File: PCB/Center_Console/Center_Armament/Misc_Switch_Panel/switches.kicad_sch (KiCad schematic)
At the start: 8 parts, among them SW1 FUEL_EXT_BTN, SW2 MASTER_TEST, SW3 RADAR_PROFILE, SW4 RADAR_RANGE, SW5 CONT_NORM, SW6 BDHI_MODE, SW7 SW_Rotary_1x5_MP

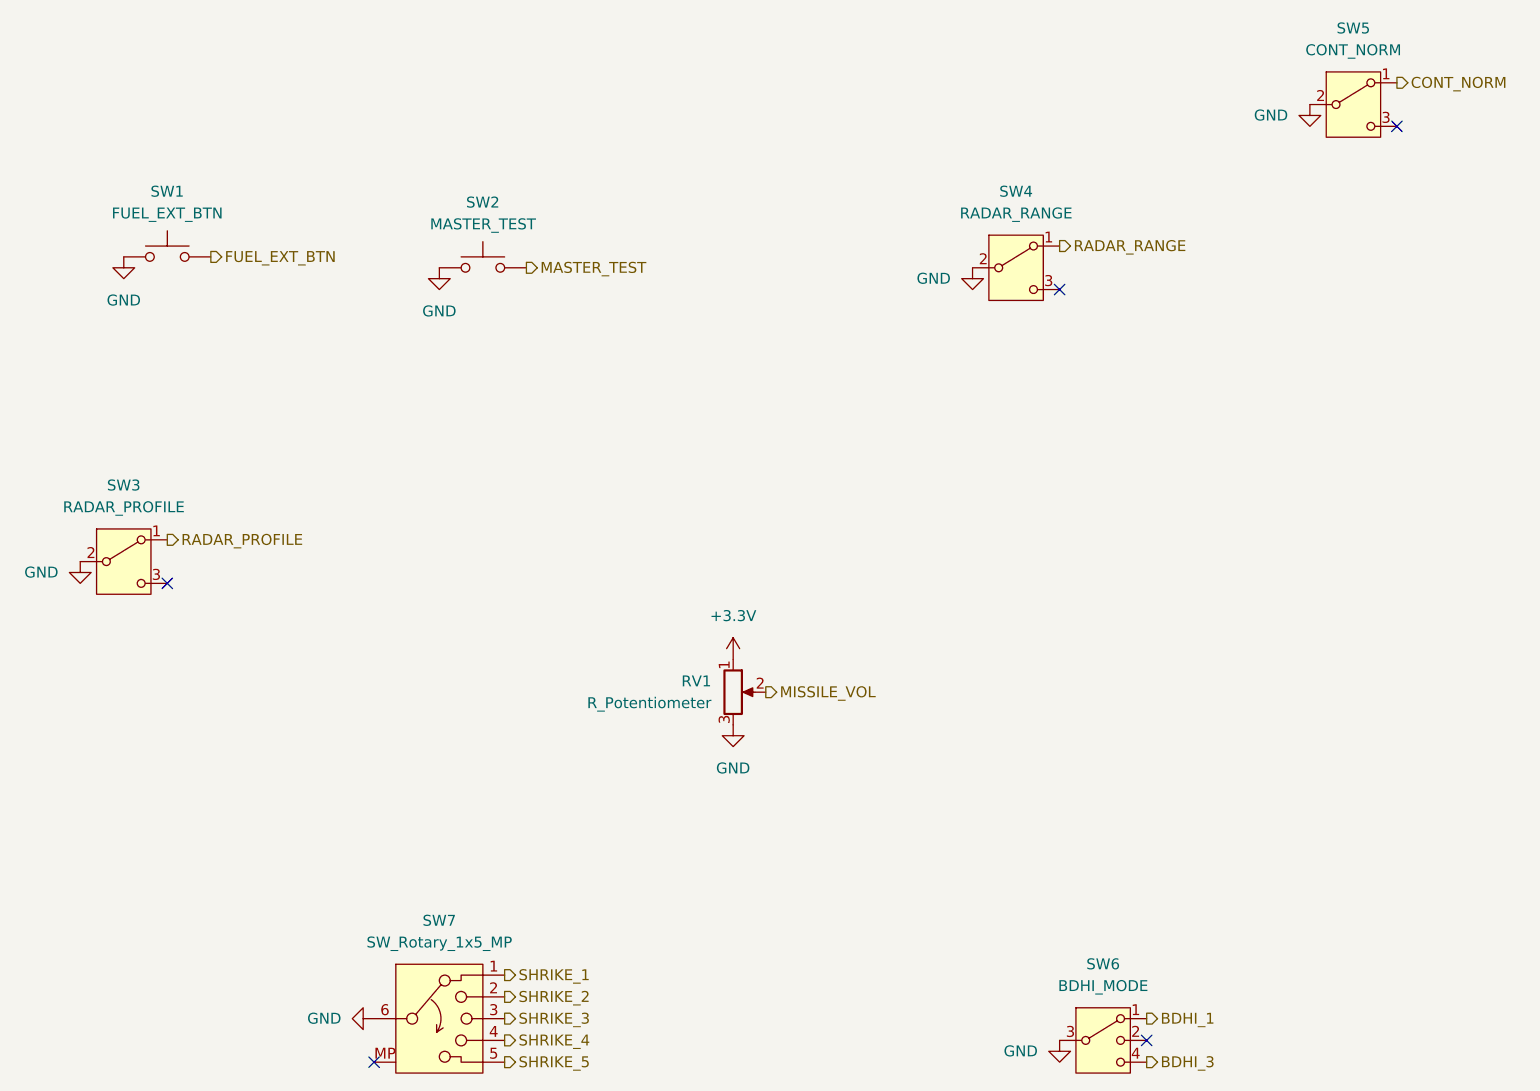
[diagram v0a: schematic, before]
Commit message: Fix LED_5050_Red symbol polarity: K=pin1, A=pin2
Symbol body was mirrored vs standard Device:LED convention — pin 1 was
labelled A and pin 2 K. Flipped triangle/bar to point left and swapped
pin names so K=1 (left) and A=2 (right), matching the generic KiCad LED
symbol.

Physical LED verified: notched/chamfered corner is the ANODE. Footprint
pad positions unchanged — pad2 (left, where the silkscreen marker sits)
is now correctly the anode. Updated kicad.md to document this.

Also includes Misc_Switch_Panel schematic edits from current KiCad session.
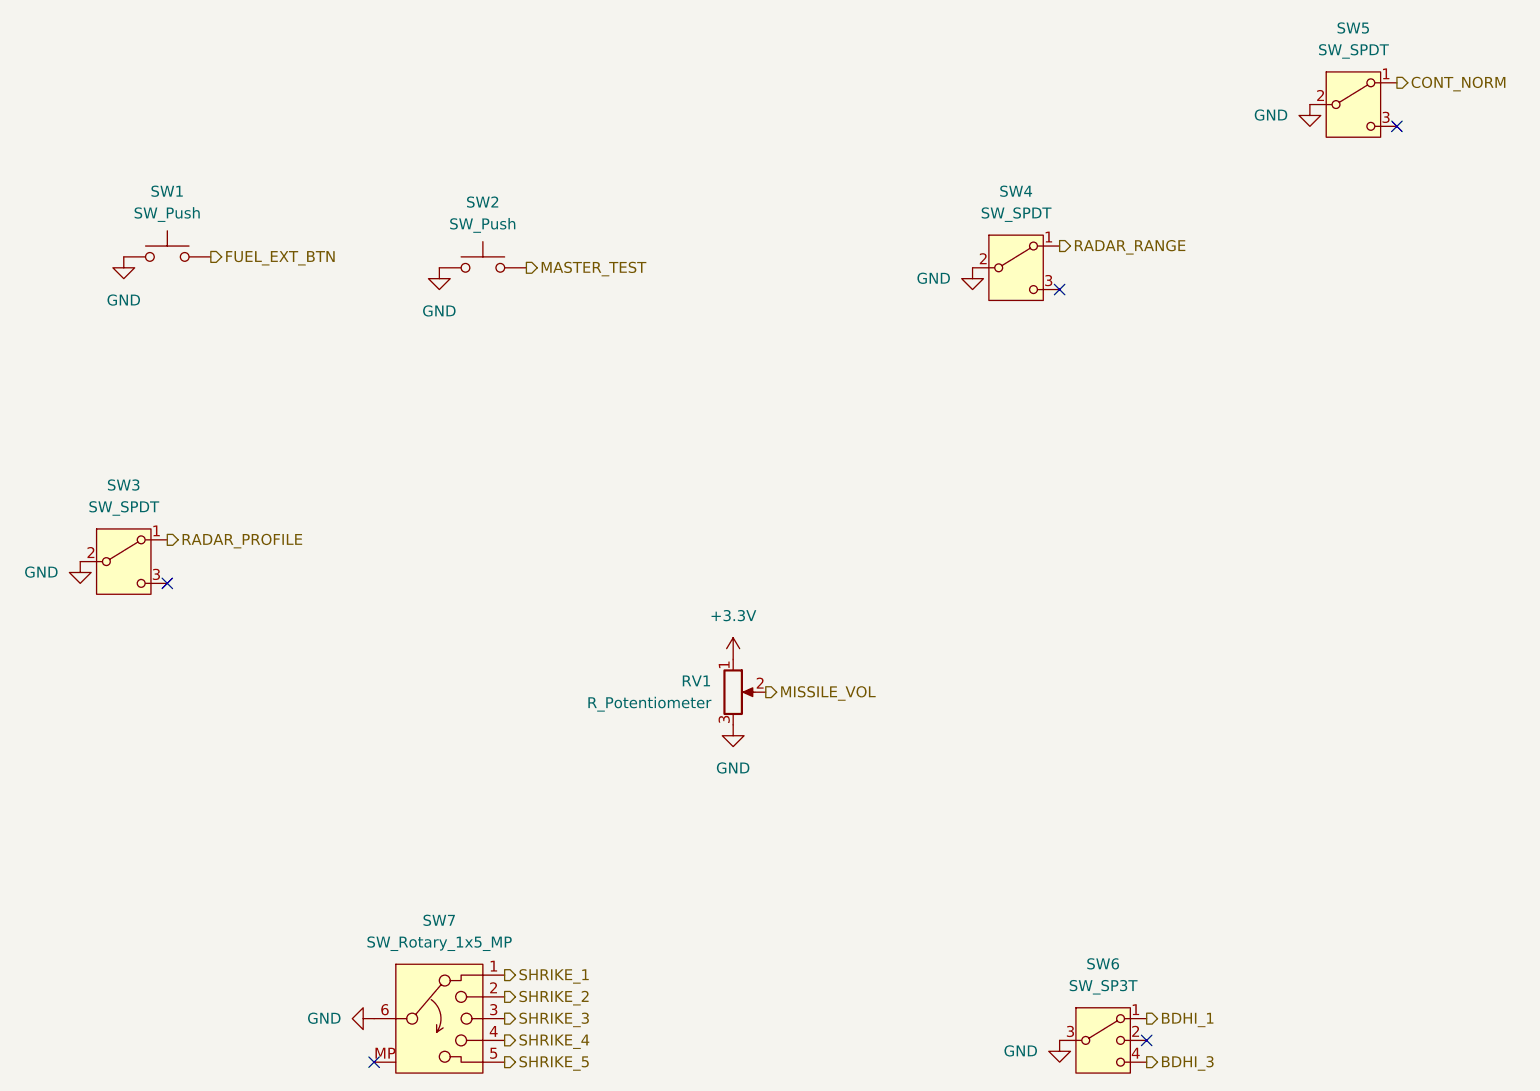
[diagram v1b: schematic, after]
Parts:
- SW1: value FUEL_EXT_BTN -> SW_Push
- SW2: value MASTER_TEST -> SW_Push
- SW3: value RADAR_PROFILE -> SW_SPDT
- SW4: value RADAR_RANGE -> SW_SPDT
- SW5: value CONT_NORM -> SW_SPDT
- SW6: value BDHI_MODE -> SW_SP3T
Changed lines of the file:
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@@
 			)
 		)
-		(property "Value" "RADAR_PROFILE"
+		(property "Value" "SW_SPDT"
 			(at 30.48 77.47 0)
 			(show_name no)
@@
 		(dnp no)
 		(fields_autoplaced yes)
-		(property "Reference" "#PWR020"
+		(property "Reference" "#PWR20"
 			(at 101.6 99.06 0)
 			(hide yes)
@@
 			(project "Misc_Switch_Panel"
 				(path "/e216e2c6-0c29-44a6-a74b-9257e68cb7df/dd445d84-0f3d-42d4-b145-d55e98d45321"
-					(reference "#PWR020")
+					(reference "#PWR20")
 					(unit 1)
 				)
@@
 			)
 		)
-		(property "Value" "RADAR_RANGE"
+		(property "Value" "SW_SPDT"
 			(at 134.62 43.18 0)
 			(show_name no)
@@
 		(dnp no)
 		(fields_autoplaced yes)
-		(property "Reference" "#PWR015"
+		(property "Reference" "#PWR15"
 			(at 129.54 55.88 0)
 			(hide yes)
@@
 			(project "Misc_Switch_Panel"
 				(path "/e216e2c6-0c29-44a6-a74b-9257e68cb7df/dd445d84-0f3d-42d4-b145-d55e98d45321"
-					(reference "#PWR015")
+					(reference "#PWR15")
 					(unit 1)
 				)
@@
 		(dnp no)
 		(fields_autoplaced yes)
-		(property "Reference" "#PWR016"
+		(property "Reference" "#PWR16"
 			(at 168.91 36.83 0)
 			(hide yes)
@@
 			(project "Misc_Switch_Panel"
 				(path "/e216e2c6-0c29-44a6-a74b-9257e68cb7df/dd445d84-0f3d-42d4-b145-d55e98d45321"
-					(reference "#PWR016")
+					(reference "#PWR16")
 					(unit 1)
 				)
@@
 			)
 		)
-		(property "Value" "BDHI_MODE"
+		(property "Value" "SW_SP3T"
 			(at 144.78 133.35 0)
 			(show_name no)
@@
 		(dnp no)
 		(fields_autoplaced yes)
-		(property "Reference" "#PWR018"
+		(property "Reference" "#PWR18"
 			(at 53.34 137.16 0)
 			(hide yes)
@@
 			(project "Misc_Switch_Panel"
 				(path "/e216e2c6-0c29-44a6-a74b-9257e68cb7df/dd445d84-0f3d-42d4-b145-d55e98d45321"
-					(reference "#PWR018")
+					(reference "#PWR18")
 					(unit 1)
 				)
@@
 			)
 		)
-		(property "Value" "MASTER_TEST"
+		(property "Value" "SW_Push"
 			(at 72.39 44.45 0)
 			(show_name no)
@@
 			)
 		)
-		(property "Value" "CONT_NORM"
+		(property "Value" "SW_SPDT"
 			(at 173.99 24.13 0)
 			(show_name no)
@@
 			)
 		)
-		(property "Value" "FUEL_EXT_BTN"
+		(property "Value" "SW_Push"
 			(at 35.56 43.18 0)
 			(show_name no)
@@
 		(dnp no)
 		(fields_autoplaced yes)
-		(property "Reference" "#PWR014"
+		(property "Reference" "#PWR14"
 			(at 25.4 90.17 0)
 			(hide yes)
@@
 			(project "Misc_Switch_Panel"
 				(path "/e216e2c6-0c29-44a6-a74b-9257e68cb7df/dd445d84-0f3d-42d4-b145-d55e98d45321"
-					(reference "#PWR014")
+					(reference "#PWR14")
 					(unit 1)
 				)
@@
 		(dnp no)
 		(fields_autoplaced yes)
-		(property "Reference" "#PWR012"
+		(property "Reference" "#PWR12"
 			(at 30.48 54.61 0)
 			(hide yes)
@@
 			(project "Misc_Switch_Panel"
 				(path "/e216e2c6-0c29-44a6-a74b-9257e68cb7df/dd445d84-0f3d-42d4-b145-d55e98d45321"
-					(reference "#PWR012")
+					(reference "#PWR12")
 					(unit 1)
 				)
@@
 		(dnp no)
 		(fields_autoplaced yes)
-		(property "Reference" "#PWR013"
+		(property "Reference" "#PWR13"
 			(at 67.31 55.88 0)
 			(hide yes)
@@
 			(project "Misc_Switch_Panel"
 				(path "/e216e2c6-0c29-44a6-a74b-9257e68cb7df/dd445d84-0f3d-42d4-b145-d55e98d45321"
-					(reference "#PWR013")
+					(reference "#PWR13")
 					(unit 1)
 				)
@@
 		(dnp no)
 		(fields_autoplaced yes)
-		(property "Reference" "#PWR019"
+		(property "Reference" "#PWR19"
 			(at 101.6 109.22 0)
 			(hide yes)
@@
 			(project "Misc_Switch_Panel"
 				(path "/e216e2c6-0c29-44a6-a74b-9257e68cb7df/dd445d84-0f3d-42d4-b145-d55e98d45321"
-					(reference "#PWR019")
+					(reference "#PWR19")
 					(unit 1)
 				)
@@
 		(dnp no)
 		(fields_autoplaced yes)
-		(property "Reference" "#PWR017"
+		(property "Reference" "#PWR17"
 			(at 139.7 146.05 0)
 			(hide yes)
@@
 			(project "Misc_Switch_Panel"
 				(path "/e216e2c6-0c29-44a6-a74b-9257e68cb7df/dd445d84-0f3d-42d4-b145-d55e98d45321"
-					(reference "#PWR017")
-					(unit 1)
-				)
+					(reference "#PWR17")
+					(unit 1)
+				)
